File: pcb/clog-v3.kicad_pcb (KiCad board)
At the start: 2 copper layers, 125.3 x 81.8 mm, 32 parts, among them J0 AudioJack4dpb, SW1 SW_Push, SW10 SW_Push, SW11 SW_Push, SW12 SW_Push, SW13 SW_Push, SW14 SW_Push, SW15 SW_Push, SW16 SW_Push, SW17 SW_Push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

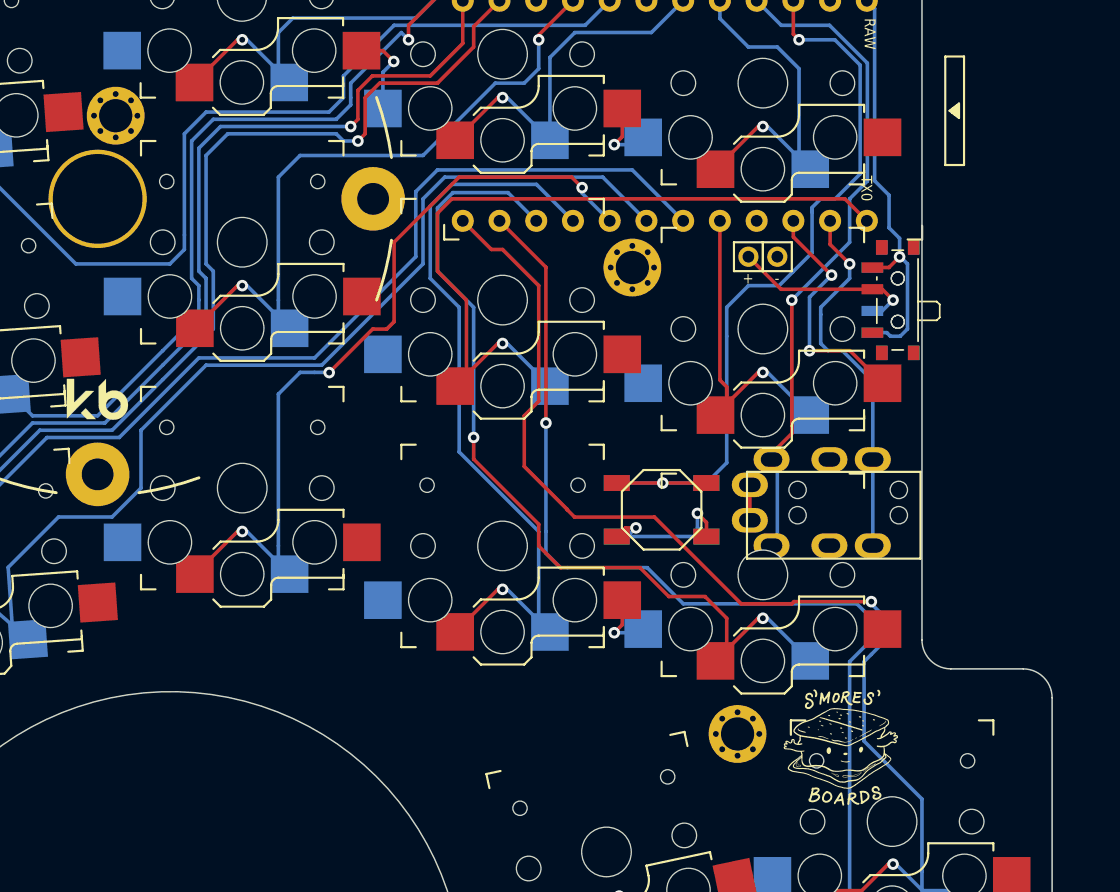
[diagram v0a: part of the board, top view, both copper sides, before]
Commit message: Update Reset Switch, Remove Holes From Plate
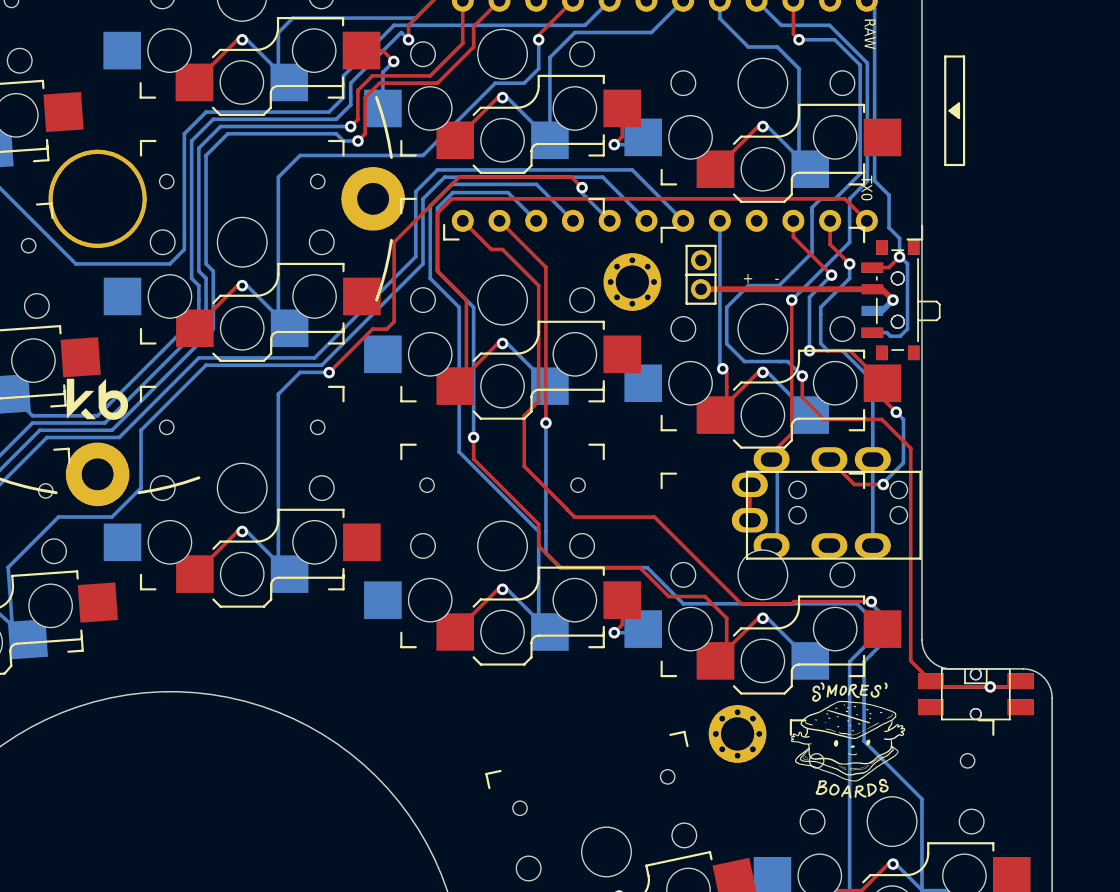
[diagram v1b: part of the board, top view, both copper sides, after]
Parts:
- removed the Ref** at (144.5, 76.5)
- SW18: footprint footprints:reset-switch-4pin -> footprints:reset-switch-angled-4pin; moved to B.Cu
- SW21: footprint footprints:reset-switch-4pin -> footprints:reset-switch-angled-4pin; moved to F.Cu
- moved SW18 25.2 mm to (204.0, 116.5), turned to 180 degrees
- moved SW21 25.2 mm to (204.0, 116.5), turned to 0 degrees
- moved -1 5.28 mm to (185.0, 86.5)
- moved +1 3.97 mm to (185.0, 88.5)
- moved Ref** 1.00 mm to (180.2, 88.0)
- moved G*** 0.71 mm to (195.0, 120.0)
- moved G*** 0.56 mm to (195.5, 120.0)
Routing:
- net RESET: track 55.4 -> 79.2 mm, vias 2 -> 3
- net BAT+: track 13.0 -> 15.3 mm
- net K10: vias 1 -> 2

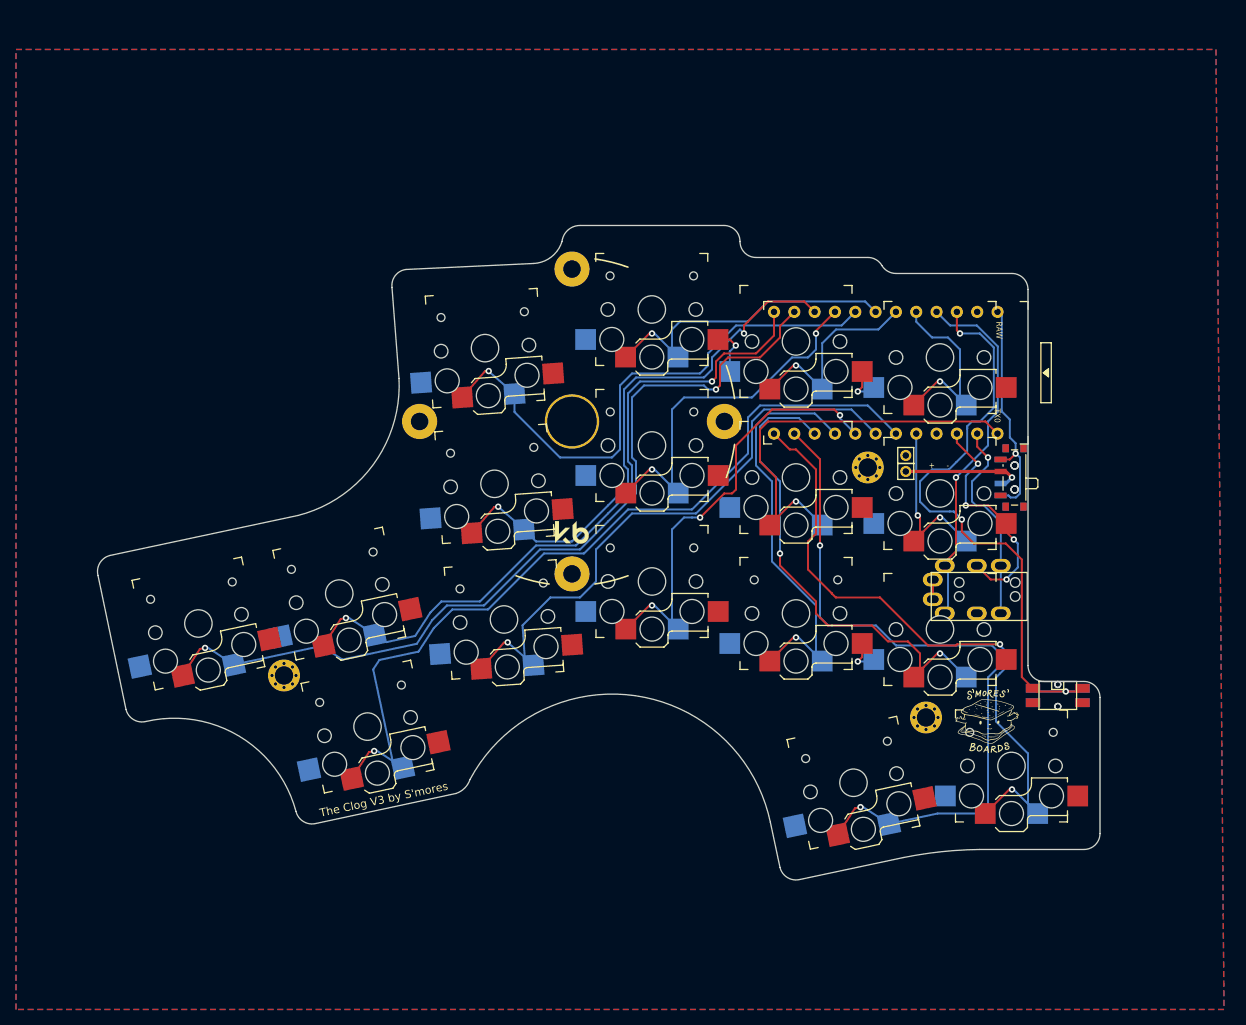
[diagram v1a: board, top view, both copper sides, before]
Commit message: Move Pinky Further Up, Rotate Thumbs Out
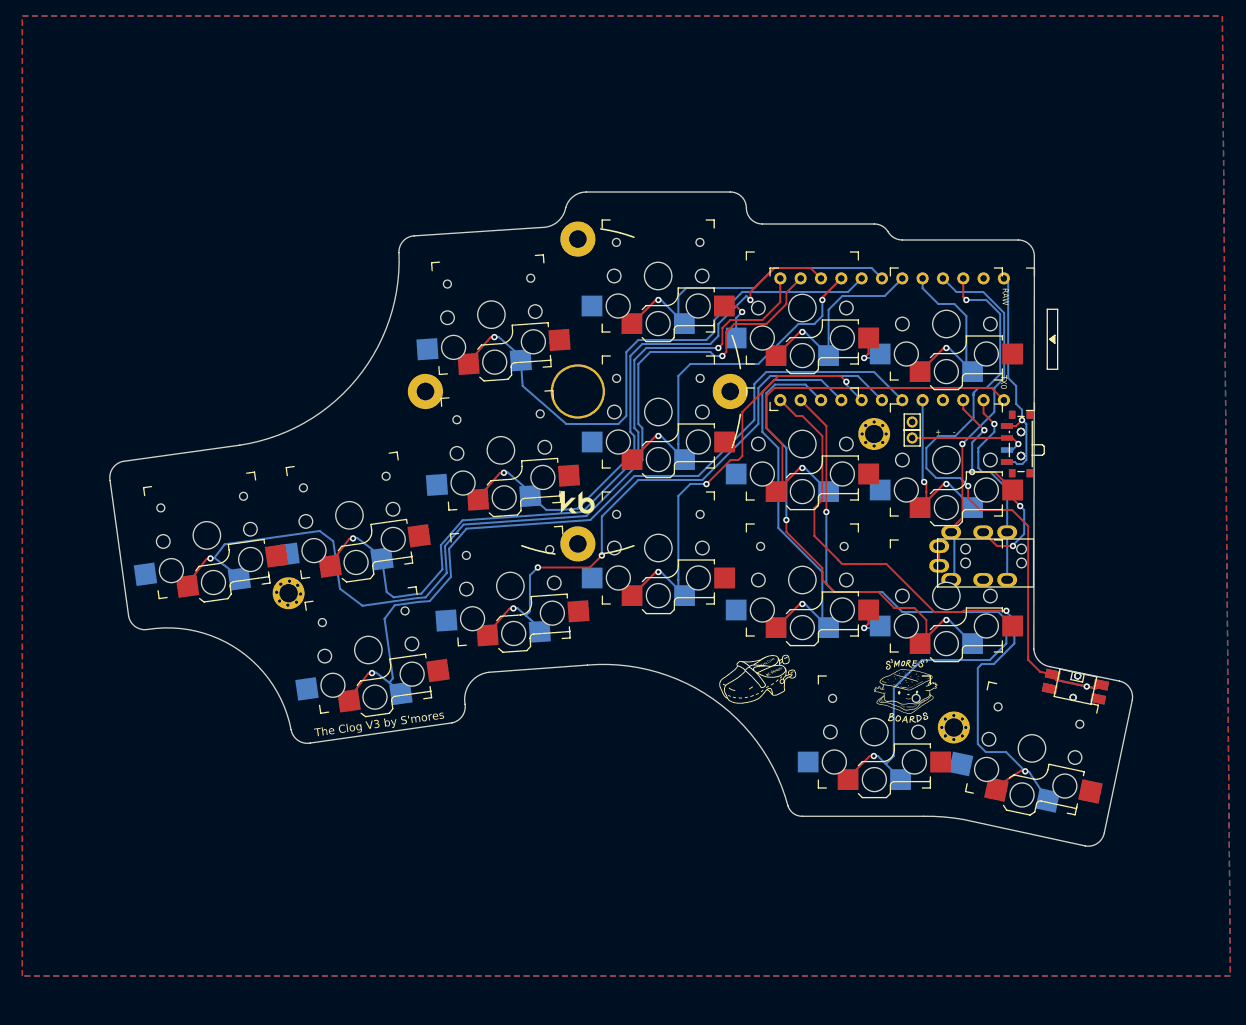
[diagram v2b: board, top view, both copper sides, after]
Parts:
- removed the G*** at (195.0, 120.0)
- removed the G*** at (195.5, 120.0)
- added G***: LOGO, art:smores, F.Cu at (184.8, 116.3)
- added G***: LOGO, art:clogs, F.Cu at (166.9, 113.9)
- added G***: LOGO, art:smores, B.Cu at (185.8, 116.3)
- added G***: LOGO, art:clogs, B.Cu at (165.9, 114.0)
- moved SW5 11.1 mm to (97.6, 96.5), turned to 8 degrees
- moved Ref** 10.3 mm to (107.9, 103.7), turned to -4 degrees
- moved SW6 9.86 mm to (115.5, 94.0), turned to 8 degrees
- moved SW11 9.57 mm to (117.8, 110.8), turned to 8 degrees
- moved SW16 6.86 mm to (181.1, 121.1), turned to 0 degrees
- moved SW3 4.26 mm to (172.1, 68.1)
- moved SW1 4.26 mm to (133.2, 68.9)
- moved SW8 4.26 mm to (154.1, 81.1)
- moved SW4 4.26 mm to (190.1, 70.1)
- moved SW13 4.26 mm to (154.1, 98.1)
- moved SW2 4.26 mm to (154.0, 64.1)
- moved SW12 4.26 mm to (135.6, 102.8)
- moved SW10 4.26 mm to (190.1, 87.1)
- moved SW7 4.26 mm to (134.4, 85.9)
- moved U1 4.26 mm to (182.8, 72.0)
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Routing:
- net K5: track 107.9 -> 119.0 mm
- net K6: track 86.9 -> 91.8 mm
- net RESET: track 79.2 -> 83.3 mm
- net K16: track 90.4 -> 87.1 mm
- net K17: track 81.4 -> 84.5 mm
- net K11: track 102.3 -> 101.2 mm
- net K1: track 69.4 -> 70.0 mm
- net K7: track 68.6 -> 69.2 mm
- net K12: track 76.1 -> 75.8 mm, vias 1 -> 3
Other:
- board size 125.3 x 81.8 mm -> 127.8 x 81.8 mm
